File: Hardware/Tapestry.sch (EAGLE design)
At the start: 101 parts, among them J1 CORTEX_DEBUGPTH, J2 POWER_JACKPTH_LOCK, U1 ATSAMS70NXXA-AN, U2 AK4618VQSFE-PACKAGE, Y1 12MHz

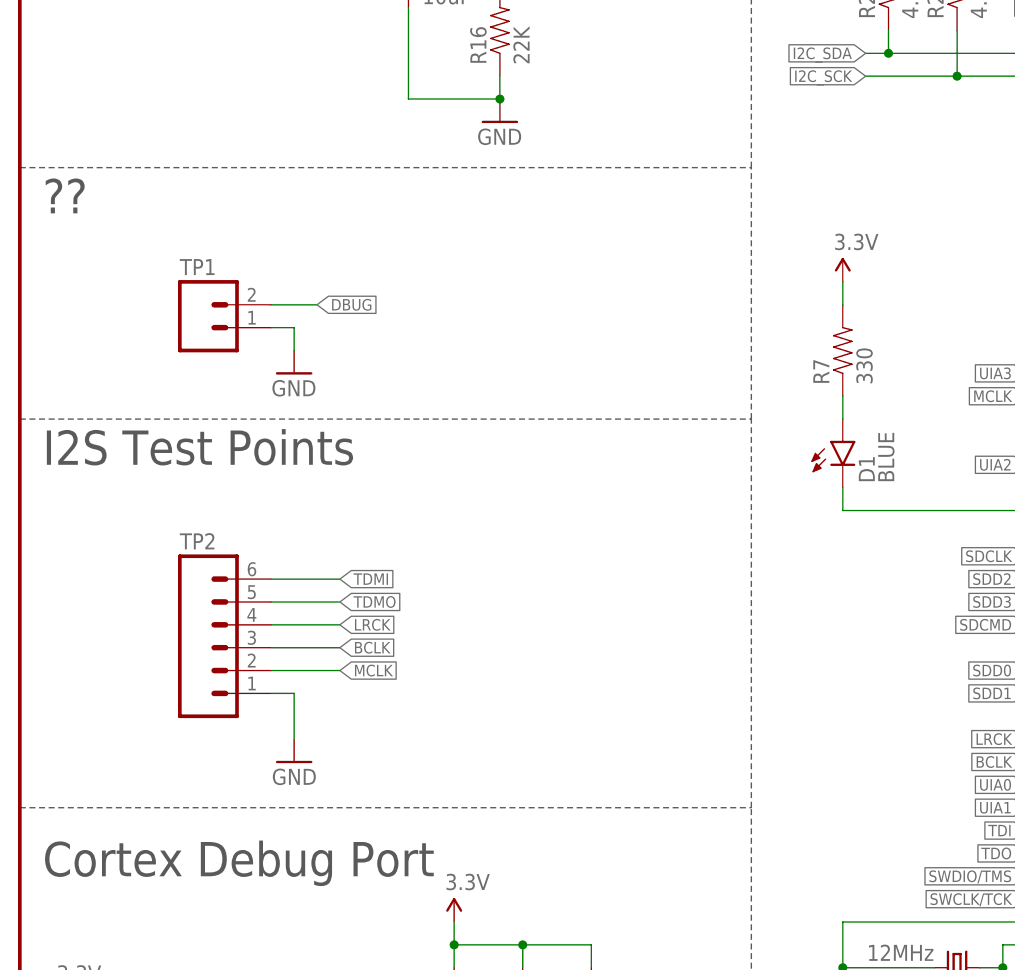
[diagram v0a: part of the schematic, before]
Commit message: Added reset switch & some labeling.
Still WIP.
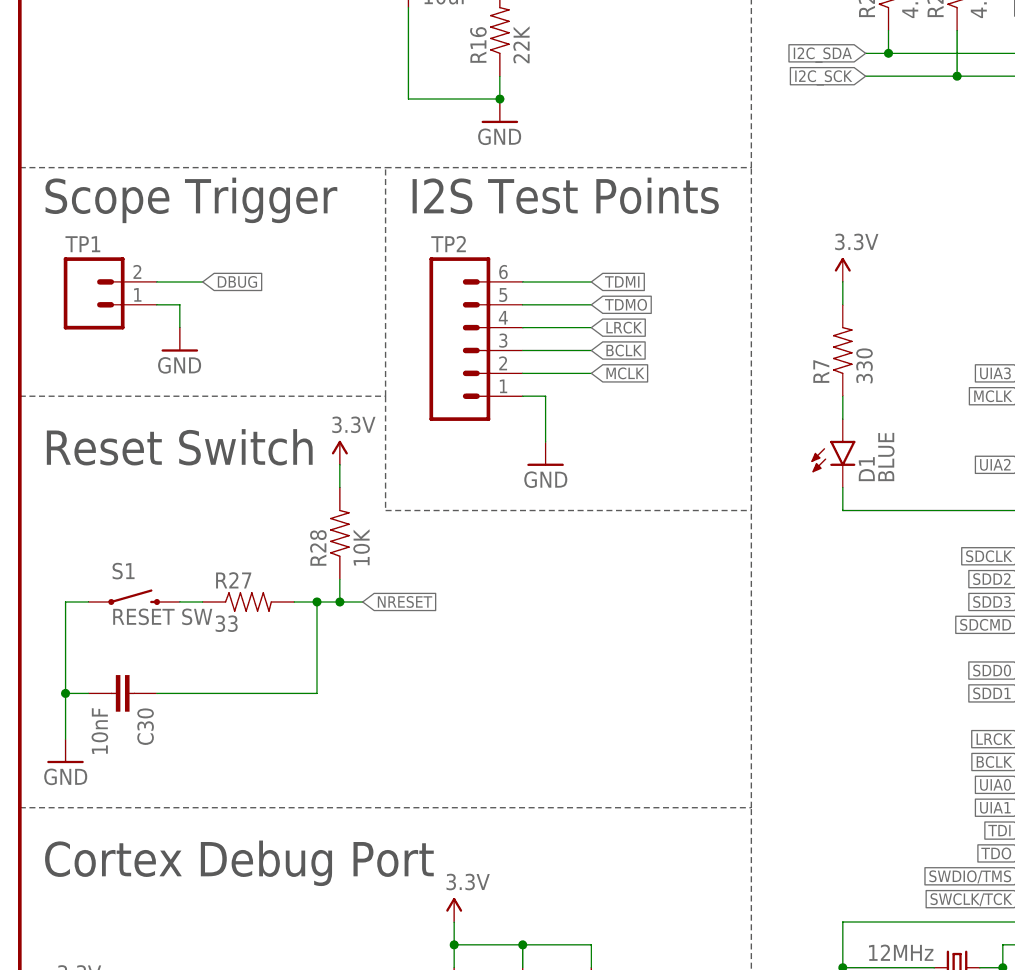
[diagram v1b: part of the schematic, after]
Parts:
- added C30: 10nF, SparkFun-Capacitors:10NF/10000PF-50V-10%(0603)
- added R27: 33, SparkFun-Resistors:33OHM1/10W1%(0603)
- added R28: 10K, SparkFun-Resistors:10KOHM-1/10W-1%(0603)0603
- added S1: RESET SW, SparkFun-Electromechanical:SWITCH-MOMENTARY-2SIDE_EZ
- JP4: device SparkFun-Connectors:M10X2NOSILK -> SparkFun-Connectors:M10X2
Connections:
- new net N$26: R27.1, S1.2
- net 3.3V: now also R28.2
- net GND: now also C30.2, S1.1
- net NRESET: now also C30.1, R27.2, R28.1
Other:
- note added: "Reset Switch"
- note added: "Scope Trigger"
- note removed: "??"
- moved on the sheet: TP1, TP2

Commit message: Continuing work.
Labeling, & sizing mostly complete.

About ready to route.
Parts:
- added S2: DNS, SparkFun-Electromechanical:SWITCH-MOMENTARY-2SIDE_EZ
- JP3: value (none) -> I/O
- JP4: value (none) -> AUDIO I/O
- S1: value RESET SW -> RESET; device SparkFun-Electromechanical:SWITCH-MOMENTARY-2SIDE_EZ -> SparkFun-Electromechanical:SWITCH-MOMENTARY-2SMD
- TP1: value (none) -> Trigger
- TP2: value (none) -> I2S TP
- TP3: value (none) -> SD TP
- U3, U4: value (none) -> LM1117
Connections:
- net GND: now also S2.1
- net N$26: now also S2.2
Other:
- note added: "S2 is optional, side-firing 6mm tact type."
- note added: "Vin range: 5 to 15 VDC"
- moved on the sheet: R18, R19, R27, R28, S1, TP2

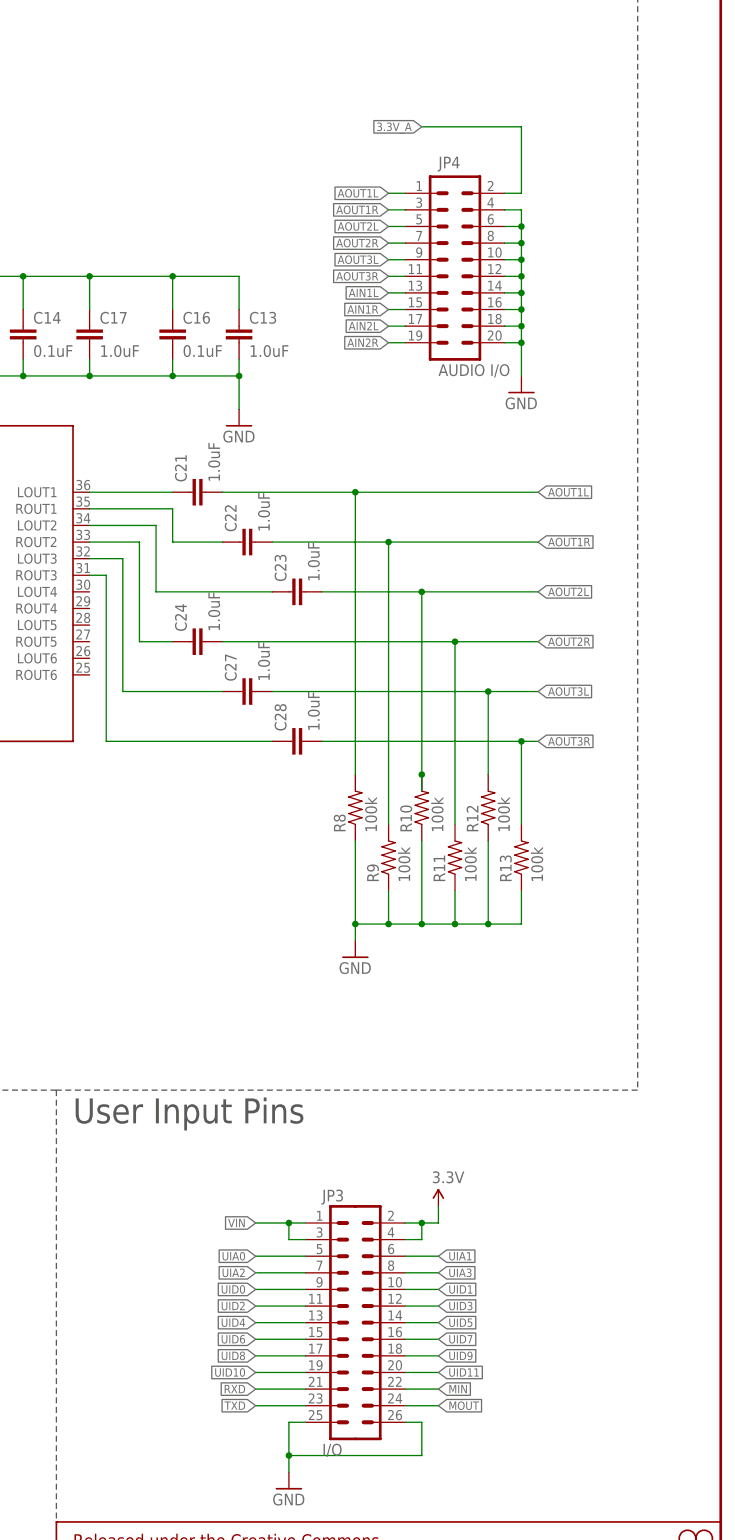
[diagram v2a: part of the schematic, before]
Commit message: Ready to start routing.
If I need to fall back, this is the one.
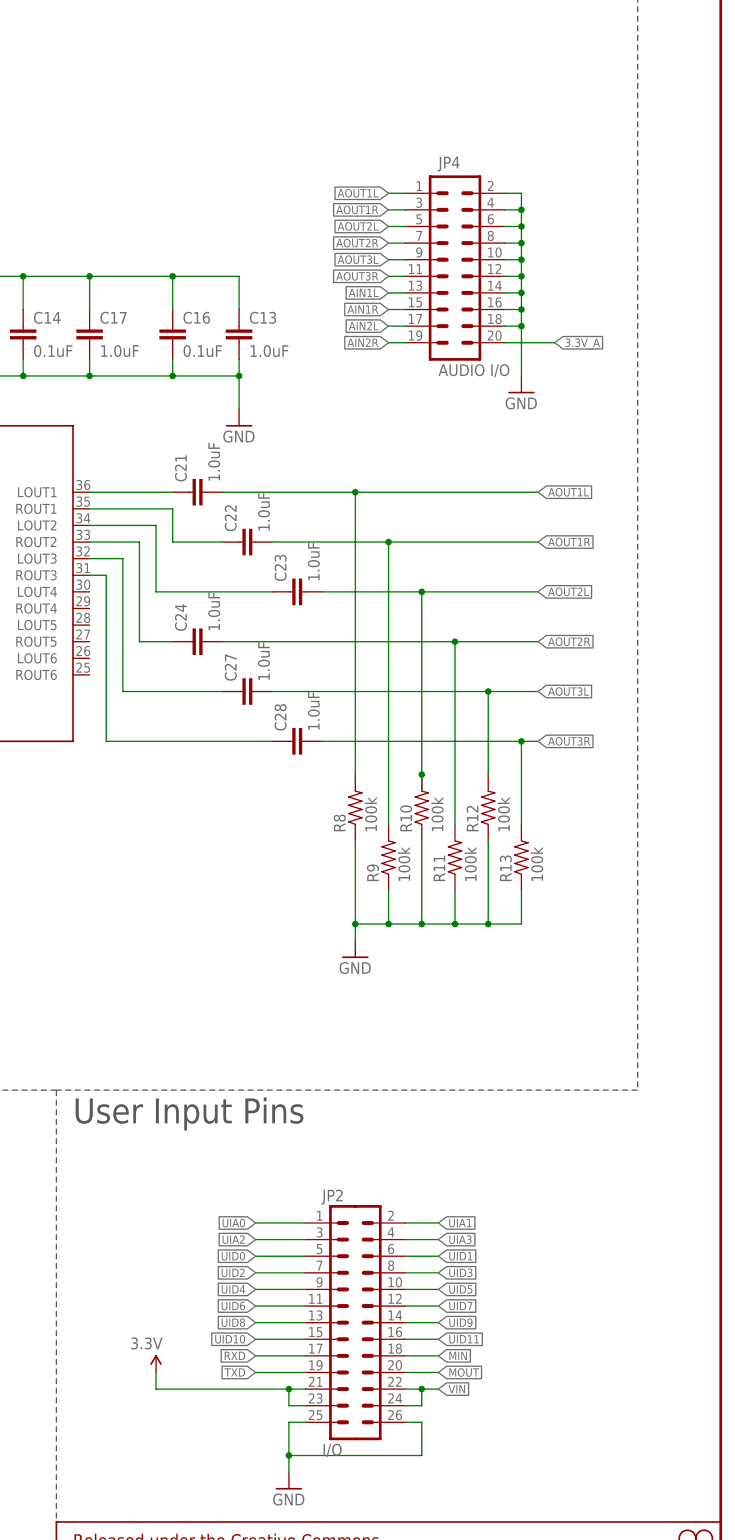
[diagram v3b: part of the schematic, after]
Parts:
- renumbered JP3 to JP2
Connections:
- net 3.3V: now also JP2.21, JP2.23; no longer JP2.2, JP2.4
- net 3.3V_A: now also JP4.20; no longer JP4.2
- net GND: now also JP4.2; no longer JP4.20
- net MIN: now also JP2.18; no longer JP2.22
- net MOUT: now also JP2.20; no longer JP2.24
- net RXD: now also JP2.17; no longer JP2.21
- net TXD: now also JP2.19; no longer JP2.23
- net UIA0: now also JP2.1; no longer JP2.5
- net UIA1: now also JP2.2; no longer JP2.6
- net UIA2: now also JP2.3; no longer JP2.7
- net UIA3: now also JP2.4; no longer JP2.8
- net UID0: now also JP2.5; no longer JP2.9
- net UID1: now also JP2.6; no longer JP2.10
- net UID10: now also JP2.15; no longer JP2.19
- net UID11: now also JP2.16; no longer JP2.20
- net UID2: now also JP2.7; no longer JP2.11
- net UID3: now also JP2.8; no longer JP2.12
- net UID4: now also JP2.9; no longer JP2.13
- net UID5: now also JP2.10; no longer JP2.14
- net UID6: now also JP2.11; no longer JP2.15
- net UID7: now also JP2.12; no longer JP2.16
- net UID8: now also JP2.13; no longer JP2.17
- net UID9: now also JP2.14; no longer JP2.18
- net VIN: now also JP2.22, JP2.24; no longer JP2.1, JP2.3

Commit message: Routing in progress.
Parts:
- added J10: 3.3V, SparkFun-Passives:TEST-POINTTP_15TH_THRU
- added J11: VIN, SparkFun-Passives:TEST-POINTTP_15TH_THRU
- added J3: AOUT4L, SparkFun-Passives:TEST-POINTTP_15TH_THRU
- added J4: AOUT4R, SparkFun-Passives:TEST-POINTTP_15TH_THRU
- added J5: AOUT5L, SparkFun-Passives:TEST-POINTTP_15TH_THRU
- added J6: AOUT5R, SparkFun-Passives:TEST-POINTTP_15TH_THRU
- added J7: AIN3R, SparkFun-Passives:TEST-POINTTP_15TH_THRU
- added J8: AIN3L, SparkFun-Passives:TEST-POINTTP_15TH_THRU
- added J9: 3.3VA, SparkFun-Passives:TEST-POINTTP_15TH_THRU
- TP2: device SparkFun-Connectors:M06NO_SILK_FEMALE_PTH -> SparkFun-Connectors:M07NO_SILK
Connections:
- new net N$28: J7.1, U2.IN6N
- new net N$30: J8.1, U2.IN5N
- new net N$31: J3.1, U2.LOUT4
- new net N$32: J4.1, U2.ROUT4
- new net N$33: J5.1, U2.LOUT5
- new net N$34: J6.1, U2.ROUT5
- net 3.3V: now also J10.1
- net 3.3V_A: now also J9.1
- net APDN: now also TP2.7
- net VIN: now also J11.1
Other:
- moved on the sheet: C21, C22, C23, C24, C27, C28, R10, R11, R12, R13, R8, R9

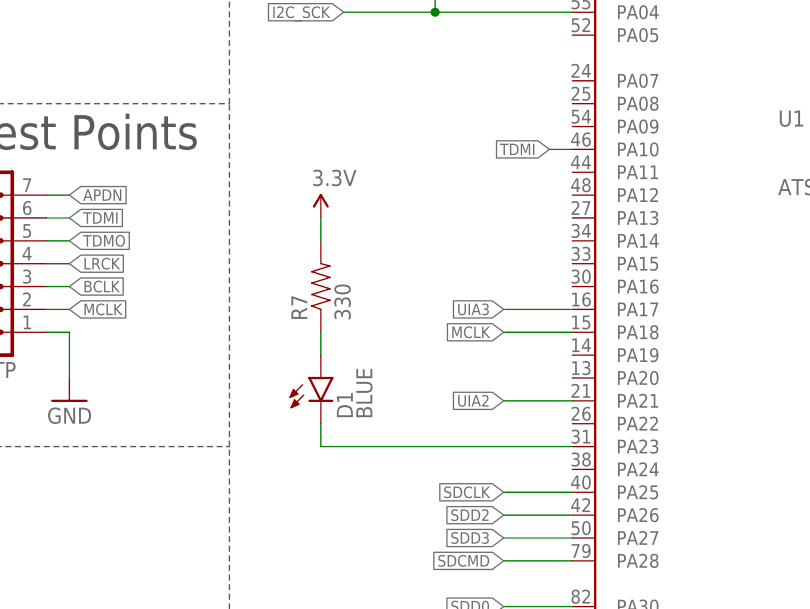
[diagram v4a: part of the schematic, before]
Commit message: Routing nearly complete.
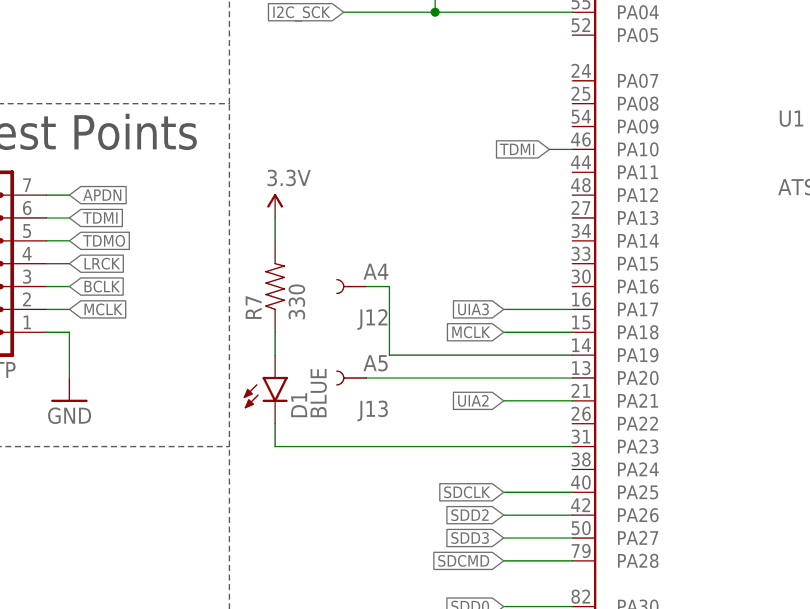
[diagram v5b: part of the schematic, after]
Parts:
- added J12: A4, SparkFun-Passives:TEST-POINTTP_15TH_THRU
- added J13: A5, SparkFun-Passives:TEST-POINTTP_15TH_THRU
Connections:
- new net N$35: J12.1, U1.PA19
- new net N$36: J13.1, U1.PA20
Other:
- moved on the sheet: D1, R7
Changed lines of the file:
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@@
 <part name="J10" library="SparkFun-Passives" deviceset="TEST-POINT" device="TP_15TH_THRU" value="3.3V"/>
 <part name="J11" library="SparkFun-Passives" deviceset="TEST-POINT" device="TP_15TH_THRU" value="VIN"/>
+<part name="J12" library="SparkFun-Passives" deviceset="TEST-POINT" device="TP_15TH_THRU" value="A4"/>
+<part name="J13" library="SparkFun-Passives" deviceset="TEST-POINT" device="TP_15TH_THRU" value="A5"/>
 </parts>
 <sheets>
@@
 <instance part="GND13" gate="1" x="287.02" y="71.12"/>
 <instance part="R6" gate="G$1" x="248.92" y="78.74" rot="R90"/>
-<instance part="R7" gate="G$1" x="91.44" y="109.22" rot="R90"/>
-<instance part="SUPPLY3" gate="G$1" x="91.44" y="116.84"/>
+<instance part="R7" gate="G$1" x="86.36" y="109.22" rot="R90"/>
+<instance part="SUPPLY3" gate="G$1" x="86.36" y="116.84"/>
 <instance part="U2" gate="G$1" x="304.8" y="180.34"/>
 <instance part="GND14" gate="1" x="358.14" y="203.2"/>
@@
 <instance part="C38" gate="G$1" x="254" y="139.7" rot="R90"/>
 <instance part="SUPPLY5" gate="G$1" x="5.08" y="35.56"/>
-<instance part="D1" gate="G$1" x="91.44" y="99.06"/>
+<instance part="D1" gate="G$1" x="86.36" y="99.06"/>
 <instance part="JP5" gate="G$1" x="292.1" y="30.48"/>
 <instance part="J1" gate="G$1" x="25.4" y="22.86"/>
@@
 <instance part="J10" gate="G$1" x="93.98" y="215.9"/>
 <instance part="J11" gate="G$1" x="27.94" y="264.16"/>
+<instance part="J12" gate="G$1" x="96.52" y="109.22" rot="R180"/>
+<instance part="J13" gate="G$1" x="96.52" y="99.06" rot="R180"/>
 </instances>
 <busses>
@@
 <pinref part="R7" gate="G$1" pin="2"/>
 <pinref part="SUPPLY3" gate="G$1" pin="3.3V"/>
-<wire x1="91.44" y1="116.84" x2="91.44" y2="114.3" width="0.1524" layer="91"/>
+<wire x1="86.36" y1="116.84" x2="86.36" y2="114.3" width="0.1524" layer="91"/>
 </segment>
 <segment>
@@
 <segment>
 <pinref part="U1" gate="G$1" pin="PA23"/>
-<wire x1="119.38" y1="91.44" x2="91.44" y2="91.44" width="0.1524" layer="91"/>
-<wire x1="91.44" y1="91.44" x2="91.44" y2="93.98" width="0.1524" layer="91"/>
+<wire x1="119.38" y1="91.44" x2="86.36" y2="91.44" width="0.1524" layer="91"/>
+<wire x1="86.36" y1="91.44" x2="86.36" y2="93.98" width="0.1524" layer="91"/>
 <pinref part="D1" gate="G$1" pin="C"/>
 </segment>
@@
 <pinref part="R7" gate="G$1" pin="1"/>
 <pinref part="D1" gate="G$1" pin="A"/>
-<wire x1="91.44" y1="104.14" x2="91.44" y2="101.6" width="0.1524" layer="91"/>
+<wire x1="86.36" y1="104.14" x2="86.36" y2="101.6" width="0.1524" layer="91"/>
 </segment>
 </net>
@@
 </segment>
 </net>
+<net name="N$35" class="0">
+<segment>
+<pinref part="U1" gate="G$1" pin="PA19"/>
+<pinref part="J12" gate="G$1" pin="1"/>
+<wire x1="96.52" y1="109.22" x2="99.06" y2="109.22" width="0.1524" layer="91"/>
+<wire x1="99.06" y1="109.22" x2="99.06" y2="101.6" width="0.1524" layer="91"/>
+<wire x1="99.06" y1="101.6" x2="119.38" y2="101.6" width="0.1524" layer="91"/>
+</segment>
+</net>
+<net name="N$36" class="0">
+<segment>
+<pinref part="U1" gate="G$1" pin="PA20"/>
+<pinref part="J13" gate="G$1" pin="1"/>
+<wire x1="96.52" y1="99.06" x2="119.38" y2="99.06" width="0.1524" layer="91"/>
+</segment>
+</net>

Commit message: Routing nearly complete.
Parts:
- added FD1, FD2: FIDUCIALUFIDUCIAL, SparkFun-Aesthetics:FIDUCIALUFIDUCIAL
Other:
- moved on the sheet: JP2

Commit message: Ready for group review.
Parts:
- added SJ3: JUMPER-PAD-2-NC_BY_TRACE, SparkFun-Passives:JUMPER-PAD-2-NC_BY_TRACE
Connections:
- net 3.3V: now also C13.1, C16.1, SJ3.1, SJ3.2, U2.TVDD
- net 3.3V_A: no longer C13.1, C16.1, U2.TVDD
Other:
- moved on the sheet: C13, C14, C16, C17, SJ1
